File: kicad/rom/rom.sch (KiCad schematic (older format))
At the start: 8 parts, among them J1 DB37_Male, U1 SST39VF200A

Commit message: Readme updates (#6)
* Readme intro section

* Board revisions for manufacturing, add digikey PNs to all, added logo.
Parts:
- J1: footprint Connector_Dsub:DSUB-37_Male_Horizontal_P2.77x2.84mm_EdgePinOffset4.94mm_Housed_MountingHolesOffset7.48mm -> Connector_Dsub:DSUB-37_Male_Horizontal_P2.77x2.84mm_EdgePinOffset7.70mm_Housed_MountingHolesOffset9.12mm; Digikey PN (none) -> AE10986-ND
- R1, R2, R3, R4: Digikey PN (none) -> P5.1KECT-ND
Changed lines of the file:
@@
 F 0 "J1" H 8568 1608 50  0000 C CNN
 F 1 "DB37_Male" H 8568 1699 50  0000 C CNN
-F 2 "Connector_Dsub:DSUB-37_Male_Horizontal_P2.77x2.84mm_EdgePinOffset4.94mm_Housed_MountingHolesOffset7.48mm" H 8650 3700 50  0001 C CNN
+F 2 "Connector_Dsub:DSUB-37_Male_Horizontal_P2.77x2.84mm_EdgePinOffset7.70mm_Housed_MountingHolesOffset9.12mm" H 8650 3700 50  0001 C CNN
 F 3 " ~" H 8650 3700 50  0001 C CNN
+F 4 "AE10986-ND" H 8650 3700 50  0001 C CNN "Digikey PN"
 	1    8650 3700
 	-1   0    0    1
@@
 F 2 "Resistor_SMD:R_1206_3216Metric" V 6640 4690 50  0001 C CNN
 F 3 "~" H 6600 4700 50  0001 C CNN
+F 4 "P5.1KECT-ND" H 6600 4700 50  0001 C CNN "Digikey PN"
 	1    6600 4700
 	1    0    0    -1
@@
 F 2 "Resistor_SMD:R_1206_3216Metric" V 4090 3390 50  0001 C CNN
 F 3 "~" H 4050 3400 50  0001 C CNN
+F 4 "P5.1KECT-ND" H 4050 3400 50  0001 C CNN "Digikey PN"
 	1    4050 3400
 	1    0    0    -1
@@
 F 2 "Resistor_SMD:R_1206_3216Metric" V 6840 2690 50  0001 C CNN
 F 3 "~" H 6800 2700 50  0001 C CNN
+F 4 "P5.1KECT-ND" H 6800 2700 50  0001 C CNN "Digikey PN"
 	1    6800 2700
 	1    0    0    -1
@@
 F 2 "Resistor_SMD:R_1206_3216Metric" V 3840 2690 50  0001 C CNN
 F 3 "~" H 3800 2700 50  0001 C CNN
+F 4 "P5.1KECT-ND" H 3800 2700 50  0001 C CNN "Digikey PN"
 	1    3800 2700
 	1    0    0    -1

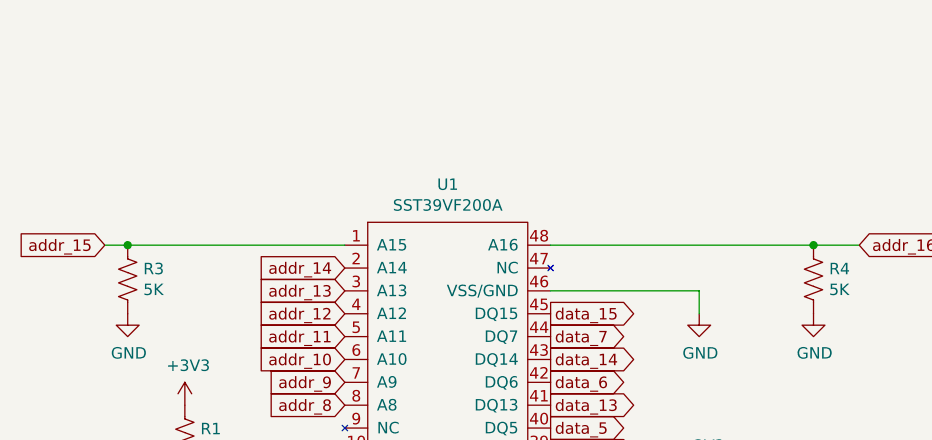
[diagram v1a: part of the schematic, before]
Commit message: Added debugger, schematic and pcb complete.
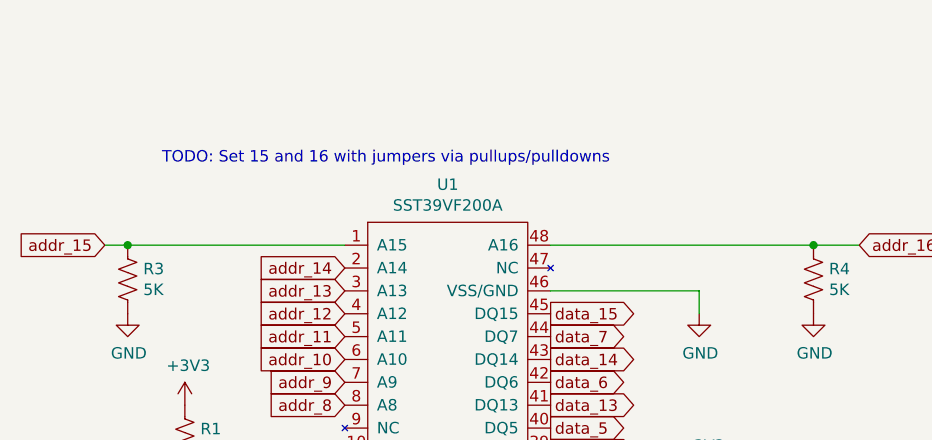
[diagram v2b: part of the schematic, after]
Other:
- note added: "TODO: Set 15 and 16 with jumpers via pullups/pulldowns"
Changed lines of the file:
@@
 Wire Wire Line
 	3800 2550 4750 2550
+Text Notes 3950 2200 0    50   ~ 0
+TODO: Set 15 and 16 with jumpers via pullups/pulldowns
 $EndSCHEMATC
